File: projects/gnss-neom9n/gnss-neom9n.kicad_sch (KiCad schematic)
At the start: 24 parts, among them J1 PWR-IN, J2 U.FL-ANT, J3 UART-I2C, J4 PPS-INT, SW1 RESET, U1 XC6206P332MR, U2 NEO-M9N-00B

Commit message: 9/6 update
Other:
- title: (none) -> GNSS NEO-M9N Breakout

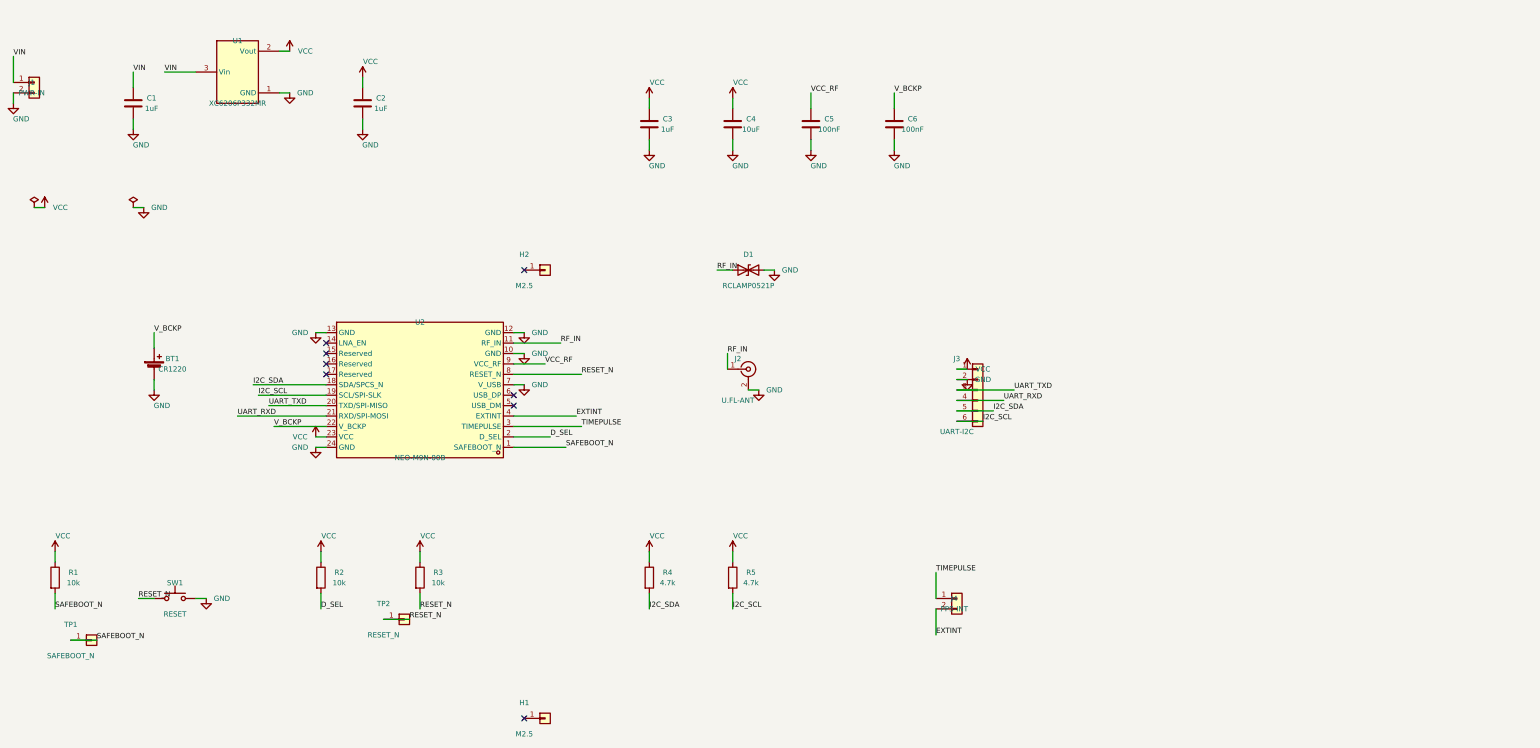
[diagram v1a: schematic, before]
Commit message: feat: promote IMU and GNSS working schematics
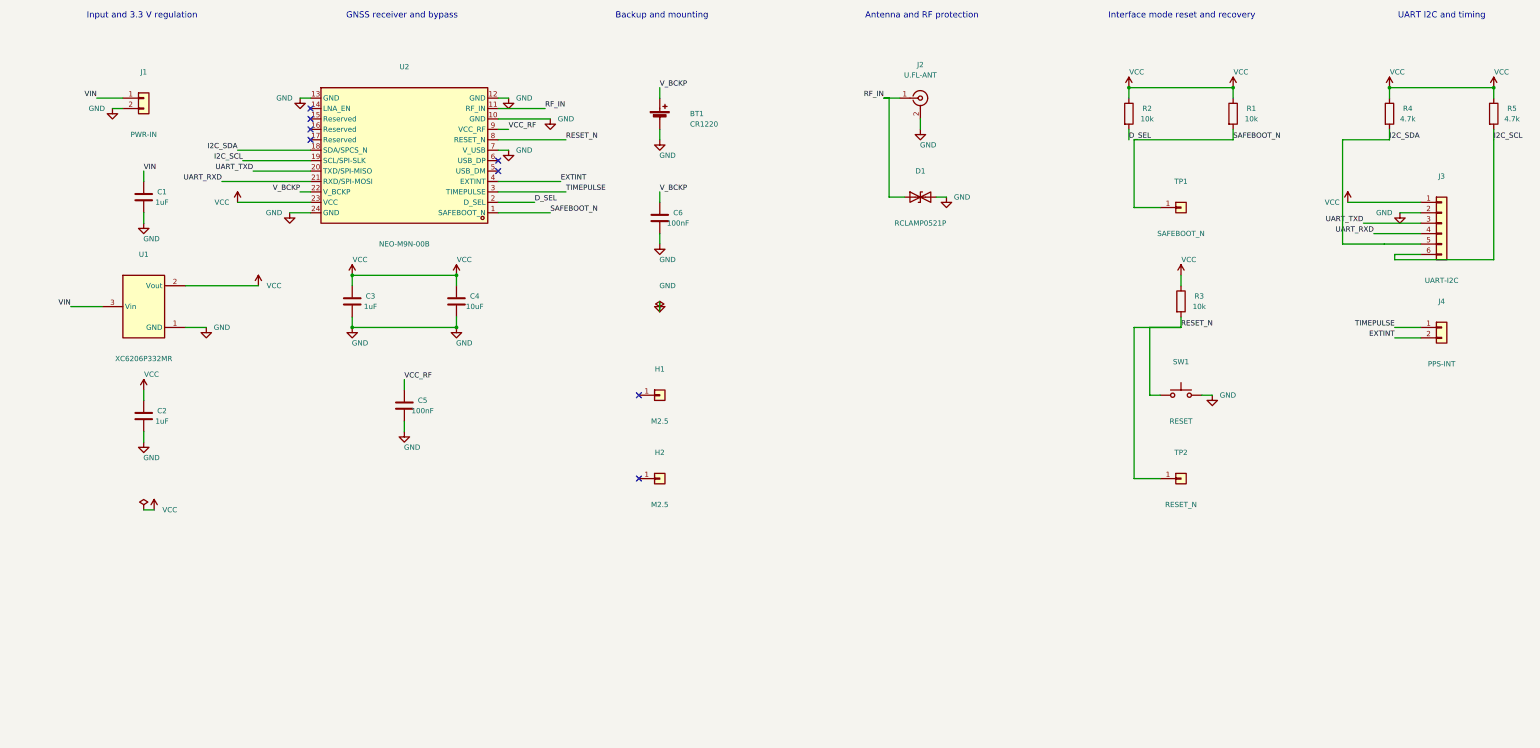
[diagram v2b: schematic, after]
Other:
- note added: "Antenna and RF protection"
- note added: "Backup and mounting"
- note added: "GNSS receiver and bypass"
- note added: "Input and 3.3 V regulation"
- note added: "Interface mode reset and recovery"
- note added: "UART I2C and timing"
- title: GNSS NEO-M9N Breakout -> NEO-M9N GNSS breakout
